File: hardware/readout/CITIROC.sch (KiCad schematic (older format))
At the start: 1 part, among them U1 CITIROC1A

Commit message: Schematic progress
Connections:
- net labels added: CCTL2, CCTL3, CCTL4, CCTL[0..4], SIPM1, SIPM10, SIPM11, SIPM12, SIPM13, SIPM14, SIPM15, SIPM16, SIPM17, SIPM18, SIPM19, SIPM2, SIPM20, SIPM21, SIPM22, SIPM23, SIPM24, SIPM25, SIPM26, SIPM27, SIPM28, SIPM29, SIPM3, SIPM30, SIPM4, SIPM5, SIPM6, SIPM7, SIPM8, SIPM9, SRCLK, SRIN, SROUT, TRIG1, TRIG10, TRIG11, TRIG12, TRIG13, TRIG14, TRIG15, TRIG16, TRIG17, TRIG18, TRIG19, TRIG2, TRIG20, TRIG21, TRIG22, TRIG23, TRIG24, TRIG25, TRIG26, TRIG27, TRIG28, TRIG29, TRIG3, TRIG30, TRIG4, TRIG5, TRIG6, TRIG7, TRIG8, TRIG9
- net labels removed: CCTL6, CCTL7, CCTL[0..7]
- wire segments 15 -> 75

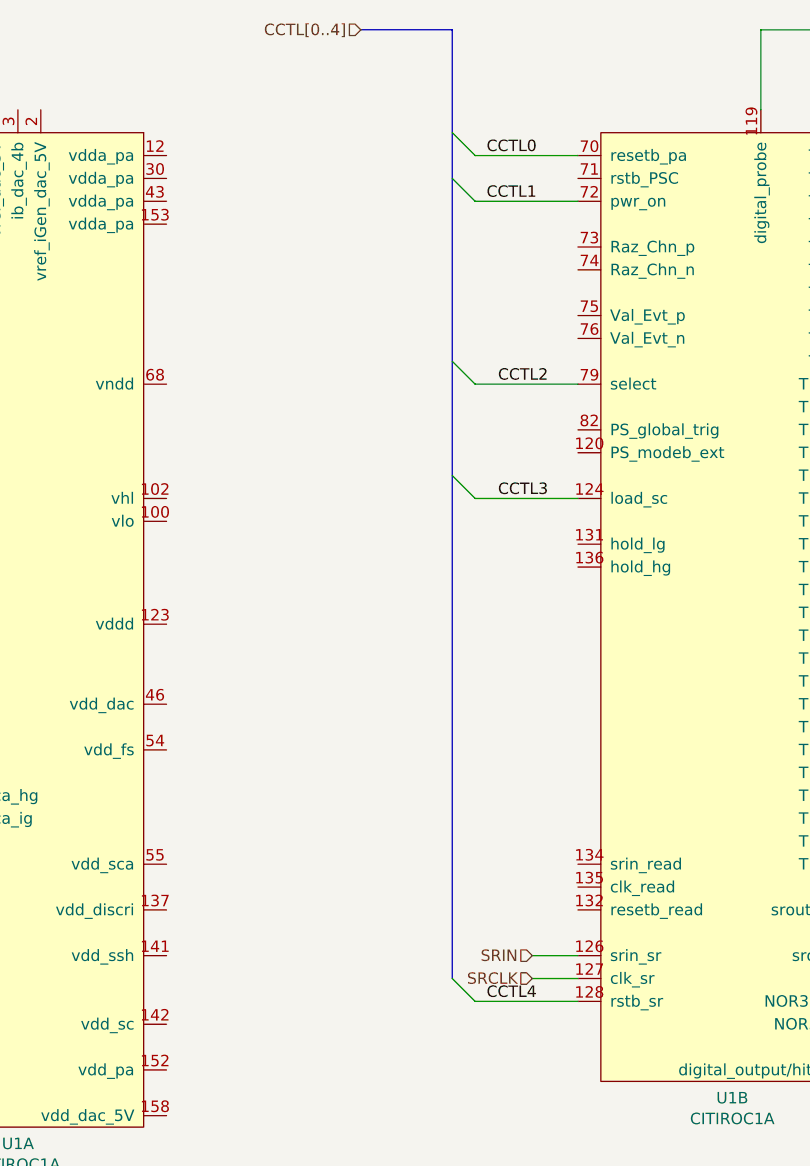
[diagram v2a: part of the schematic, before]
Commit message: Readout schem heirarchy almost done
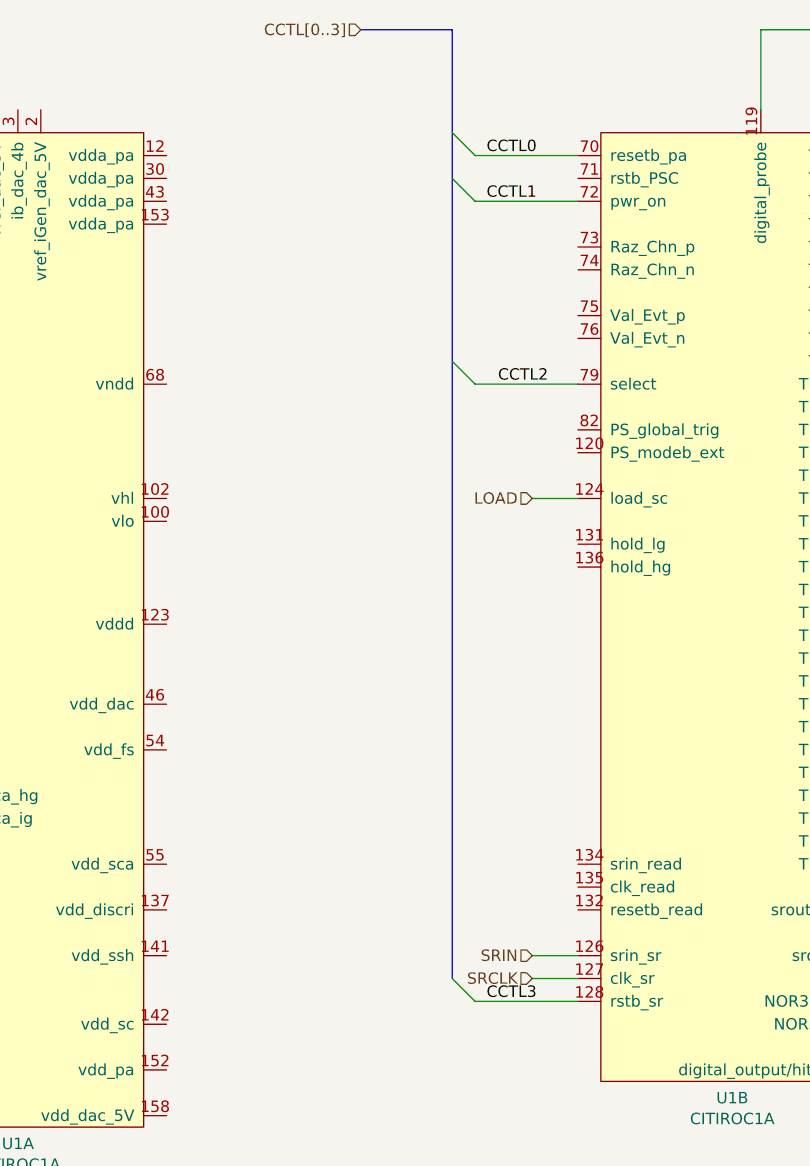
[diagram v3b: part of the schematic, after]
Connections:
- net CCTL4 is gone; now on net CCTL3: U1.128 (rstb_sr)
- net CCTL3: no longer U1.124 (load_sc)
- new net LOAD: U1.124 (load_sc)
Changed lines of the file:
@@
 $Descr A4 11693 8268
 encoding utf-8
-Sheet 7 31
+Sheet 9 35
 Title ""
 Date ""
@@
 AR Path="/6109CA1E/610DA535/61017738" Ref="U?"  Part="1"
 AR Path="/6109CA1E/610DA544/61017738" Ref="U?"  Part="1"
+AR Path="/613830F1/61017738" Ref="U?"  Part="1"
+AR Path="/61383376/613835C6/61017738" Ref="U?"  Part="1"
+AR Path="/61383376/61383667/61017738" Ref="U?"  Part="1"
+AR Path="/61383376/61383758/61017738" Ref="U?"  Part="1"
+AR Path="/610F1616/613835C6/61017738" Ref="U?"  Part="1"
+AR Path="/610F1616/61383667/61017738" Ref="U?"  Part="1"
+AR Path="/610F1616/61383758/61017738" Ref="U?"  Part="1"
+AR Path="/61119E97/613835C6/61017738" Ref="U?"  Part="1"
+AR Path="/61119E97/61383667/61017738" Ref="U?"  Part="1"
+AR Path="/61119E97/61383758/61017738" Ref="U?"  Part="1"
+AR Path="/61119EA4/613835C6/61017738" Ref="U?"  Part="1"
+AR Path="/61119EA4/61383667/61017738" Ref="U?"  Part="1"
+AR Path="/61119EA4/61383758/61017738" Ref="U?"  Part="1"
+AR Path="/6111A893/613835C6/61017738" Ref="U?"  Part="1"
+AR Path="/6111A893/61383667/61017738" Ref="U?"  Part="1"
+AR Path="/6111A893/61383758/61017738" Ref="U?"  Part="1"
+AR Path="/6111A8A0/613835C6/61017738" Ref="U?"  Part="1"
+AR Path="/6111A8A0/61383667/61017738" Ref="U?"  Part="1"
+AR Path="/6111A8A0/61383758/61017738" Ref="U?"  Part="1"
 F 0 "U?" V 8423 3100 50  0000 C CNN
 F 1 "CITIROC1A" V 8514 3100 50  0000 C CNN
@@
 AR Path="/6109CA1E/610DA535/6101A264" Ref="U?"  Part="2"
 AR Path="/6109CA1E/610DA544/6101A264" Ref="U?"  Part="2"
+AR Path="/613830F1/6101A264" Ref="U?"  Part="2"
+AR Path="/61383376/613835C6/6101A264" Ref="U?"  Part="2"
+AR Path="/61383376/61383667/6101A264" Ref="U?"  Part="2"
+AR Path="/61383376/61383758/6101A264" Ref="U?"  Part="2"
+AR Path="/610F1616/613835C6/6101A264" Ref="U?"  Part="2"
+AR Path="/610F1616/61383667/6101A264" Ref="U?"  Part="2"
+AR Path="/610F1616/61383758/6101A264" Ref="U?"  Part="2"
+AR Path="/61119E97/613835C6/6101A264" Ref="U?"  Part="2"
+AR Path="/61119E97/61383667/6101A264" Ref="U?"  Part="2"
+AR Path="/61119E97/61383758/6101A264" Ref="U?"  Part="2"
+AR Path="/61119EA4/613835C6/6101A264" Ref="U?"  Part="2"
+AR Path="/61119EA4/61383667/6101A264" Ref="U?"  Part="2"
+AR Path="/61119EA4/61383758/6101A264" Ref="U?"  Part="2"
+AR Path="/6111A893/613835C6/6101A264" Ref="U?"  Part="2"
+AR Path="/6111A893/61383667/6101A264" Ref="U?"  Part="2"
+AR Path="/6111A893/61383758/6101A264" Ref="U?"  Part="2"
+AR Path="/6111A8A0/613835C6/6101A264" Ref="U?"  Part="2"
+AR Path="/6111A8A0/61383667/6101A264" Ref="U?"  Part="2"
+AR Path="/6111A8A0/61383758/6101A264" Ref="U?"  Part="2"
 F 0 "U?" H 8725 -2723 50  0000 C CNN
 F 1 "CITIROC1A" H 8725 -2814 50  0000 C CNN
@@
 AR Path="/6109CA1E/610DA535/6101D6C7" Ref="U?"  Part="3"
 AR Path="/6109CA1E/610DA544/6101D6C7" Ref="U?"  Part="3"
+AR Path="/613830F1/6101D6C7" Ref="U?"  Part="3"
+AR Path="/61383376/613835C6/6101D6C7" Ref="U?"  Part="3"
+AR Path="/61383376/61383667/6101D6C7" Ref="U?"  Part="3"
+AR Path="/61383376/61383758/6101D6C7" Ref="U?"  Part="3"
+AR Path="/610F1616/613835C6/6101D6C7" Ref="U?"  Part="3"
+AR Path="/610F1616/61383667/6101D6C7" Ref="U?"  Part="3"
+AR Path="/610F1616/61383758/6101D6C7" Ref="U?"  Part="3"
+AR Path="/61119E97/613835C6/6101D6C7" Ref="U?"  Part="3"
+AR Path="/61119E97/61383667/6101D6C7" Ref="U?"  Part="3"
+AR Path="/61119E97/61383758/6101D6C7" Ref="U?"  Part="3"
+AR Path="/61119EA4/613835C6/6101D6C7" Ref="U?"  Part="3"
+AR Path="/61119EA4/61383667/6101D6C7" Ref="U?"  Part="3"
+AR Path="/61119EA4/61383758/6101D6C7" Ref="U?"  Part="3"
+AR Path="/6111A893/613835C6/6101D6C7" Ref="U?"  Part="3"
+AR Path="/6111A893/61383667/6101D6C7" Ref="U?"  Part="3"
+AR Path="/6111A893/61383758/6101D6C7" Ref="U?"  Part="3"
+AR Path="/6111A8A0/613835C6/6101D6C7" Ref="U?"  Part="3"
+AR Path="/6111A8A0/61383667/6101D6C7" Ref="U?"  Part="3"
+AR Path="/6111A8A0/61383758/6101D6C7" Ref="U?"  Part="3"
 F 0 "U?" H 2800 -1323 50  0000 C CNN
 F 1 "CITIROC1A" H 2800 -1414 50  0000 C CNN
@@
 	9400 5100 9800 5100
 Wire Wire Line
-	8050 3100 7600 3100
-Wire Wire Line
 	8050 2600 7600 2600
 Wire Wire Line
@@
 CCTL1
 Text Label 7650 5300 0    50   ~ 0
-CCTL4
+CCTL3
 Entry Wire Line
 	7500 1500 7600 1600
@@
 Entry Wire Line
 	7500 2500 7600 2600
-Entry Wire Line
-	7500 3000 7600 3100
 Entry Wire Line
 	7500 5200 7600 5300
@@
 	7500 1050 7100 1050
 Text HLabel 7100 1050 0    50   Input ~ 0
-CCTL[0..4]
+CCTL[0..3]
 Wire Wire Line
 	3450 3700 3750 3700
@@
 Wire Wire Line
 	7850 5100 8050 5100
+Text Label 7700 2600 0    50   ~ 0
+CCTL2
+Wire Wire Line
+	8050 3100 7850 3100
+Text HLabel 7850 3100 0    50   Input ~ 0
+LOAD
 Wire Bus Line
 	7500 1050 7500 5200
@@
 Wire Bus Line
 	1550 1800 1550 5100
-Text Label 7700 2600 0    50   ~ 0
-CCTL2
-Text Label 7700 3100 0    50   ~ 0
-CCTL3
 $EndSCHEMATC

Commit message: schematic in progress
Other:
- note added: "EMPHATIC readout board\nCITIROC ASIC -- 1 of 18"
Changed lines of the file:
@@
 $Descr A4 11693 8268
 encoding utf-8
-Sheet 9 35
+Sheet 9 38
 Title ""
 Date ""
@@
 Wire Bus Line
 	1550 1800 1550 5100
+Text Notes 7050 6850 0    75   ~ 0
+EMPHATIC readout board\nCITIROC ASIC -- 1 of 18
 $EndSCHEMATC

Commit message: working on schematic
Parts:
- added C? (x4): 1.0uF, symbol Device:C_Small
- added C? (x20): 0.1uF, symbol Device:C_Small
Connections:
- net labels added: +1V8A, +3.3V, +3.3VA, +5V, GND
- wire segments 75 -> 236

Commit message: working on schematic
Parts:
- gave numbers to parts that had none: 24
- renumbered U1 to U4
